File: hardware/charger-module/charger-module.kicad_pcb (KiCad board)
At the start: 4 copper layers, 80 x 24.3 mm, 74 parts, among them J1 Bus_PCI_Express_x1, J2 Conn_01x06_Pin, J3 RP_USB, J4 USB_C_Receptacle_USB2.0_14P, SW1 BOOT, SW2 RESET, U1 AMS1117-3.3, U2 W25Q32JVSSIQ, U3 RP2040, U4 MPQ4242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

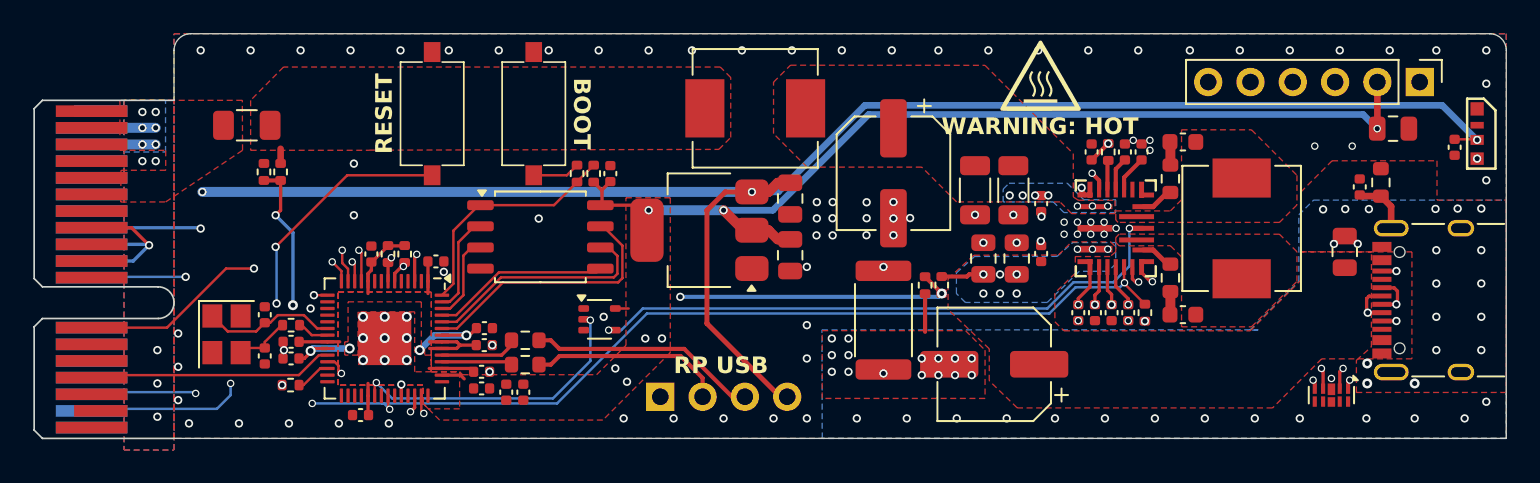
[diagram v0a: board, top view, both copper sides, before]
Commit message: feat: split i2c network
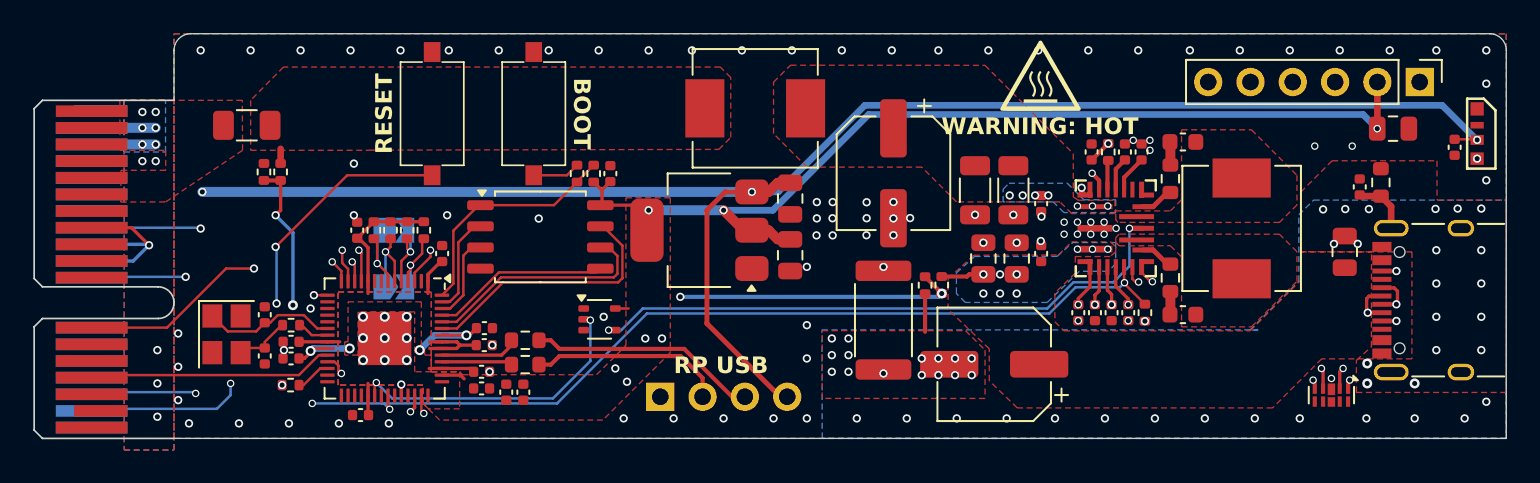
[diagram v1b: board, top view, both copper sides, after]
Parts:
- added JP1: SDA_Jumper, Jumper:SolderJumper-2_P1.3mm_Open_TrianglePad1.0x1.5mm, B.Cu at (47.2, 41.2)
- added JP2: SCL_Jumper, Jumper:SolderJumper-2_P1.3mm_Open_TrianglePad1.0x1.5mm, B.Cu at (47.2, 37.8)
- added R19: 10K, Resistor_SMD:R_0402_1005Metric, F.Cu at (49.0, 37.8)
- added R20: 10K, Resistor_SMD:R_0402_1005Metric, F.Cu at (48.0, 37.8)
- moved C24 1.66 mm to (45.0, 37.8)
- moved R12 1.66 mm to (47.0, 37.8)
- moved R13 1.66 mm to (46.0, 37.8)
- moved C18 0.61 mm to (50.1, 39.2), turned to 90 degrees
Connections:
- net LED_DIN renamed /LED_DIN
- J1 pad A8: SDA -> /SDA_IN
- J1 pad B12: SCL -> /SCL_IN
- R12 pad 2: SDA -> /SDA_IN
- R13 pad 2: SCL -> /SCL_IN
- U3 pad 4: /GPIO2 -> /SDA_OUT
- U3 pad 5: /GPIO3 -> /SCL_OUT
- U3 pad 6: SDA -> /SDA_IN
- U3 pad 7: SCL -> /SCL_IN
- U4 pad 10: SCL -> /SCL_OUT
- U4 pad 9: SDA -> /SDA_OUT
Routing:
- net SCL: track 82.2 -> 0.00 mm, vias 3 -> 0
- net SDA: track 81.4 -> 0.00 mm, vias 3 -> 0
- net /SCL_OUT: track 0.00 -> 63.9 mm, vias 0 -> 2
- net /SDA_OUT: track 0.00 -> 63.9 mm, vias 0 -> 2
- net /SDA_IN: track 0.00 -> 25.1 mm, vias 0 -> 2
- net /SCL_IN: track 0.00 -> 23.9 mm, vias 0 -> 2
- net +3.3V: track 77.0 -> 81.1 mm
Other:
- board text added: "I2C Combine"

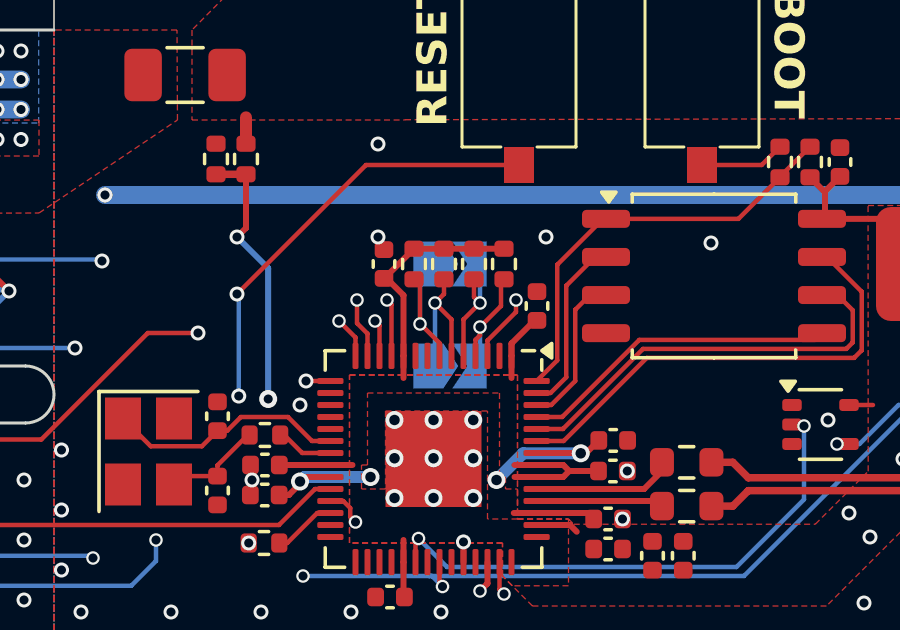
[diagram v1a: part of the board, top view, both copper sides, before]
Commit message: chore: switch jumper footprints
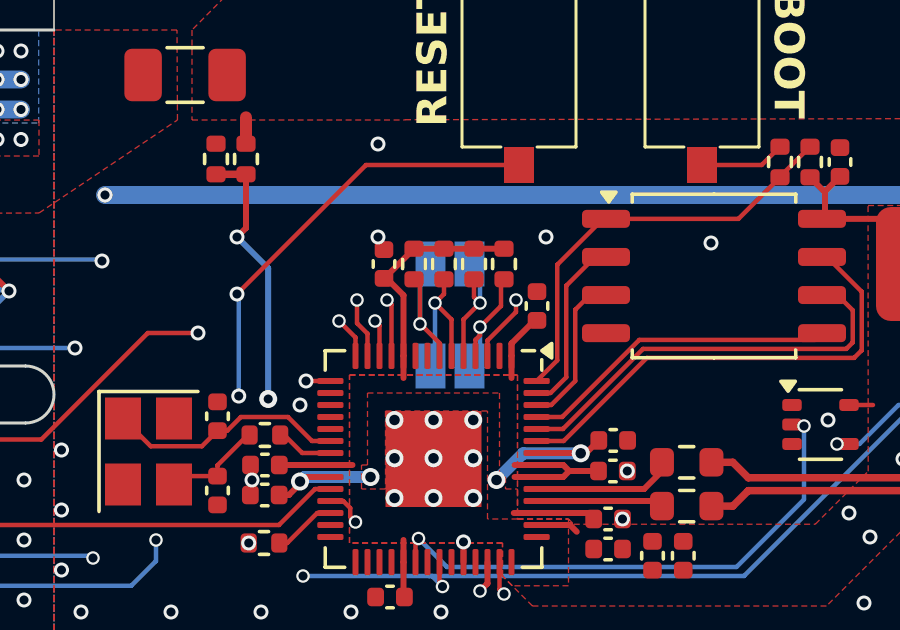
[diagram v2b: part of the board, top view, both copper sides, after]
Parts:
- JP1, JP2: footprint Jumper:SolderJumper-2_P1.3mm_Open_TrianglePad1.0x1.5mm -> Jumper:SolderJumper-2_P1.3mm_Open_Pad1.0x1.5mm
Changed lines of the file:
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@@
 		)
 	)
-	(footprint "Jumper:SolderJumper-2_P1.3mm_Open_TrianglePad1.0x1.5mm"
+	(footprint "Jumper:SolderJumper-2_P1.3mm_Open_Pad1.0x1.5mm"
 		(layer "B.Cu")
 		(at 47.2 37.8)
-		(descr "SMD Solder Jumper, 1x1.5mm Triangular Pads, 0.3mm gap, open")
+		(descr "SMD Solder Jumper, 1x1.5mm Pads, 0.3mm gap, open")
 		(tags "solder jumper open")
 		(property "Reference" "JP2"
-			(at 0 1.8 360)
-			(layer "B.SilkS")
-			(hide yes)
+			(at 0 1.8 180)
+			(layer "B.SilkS")
 			(effects
 				(font
@@
 		)
 		(property "Value" "SCL_Jumper"
-			(at 0 -1.9 360)
-			(layer "B.Fab")
-			(effects
-				(font
-					(size 1 1)
-					(thickness 0.15)
-				)
-				(justify mirror)
-			)
-		)
-		(property "Footprint" "Jumper:SolderJumper-2_P1.3mm_Open_TrianglePad1.0x1.5mm"
+			(at 0 -1.9 180)
+			(layer "B.Fab")
+			(effects
+				(font
+					(size 1 1)
+					(thickness 0.15)
+				)
+				(justify mirror)
+			)
+		)
+		(property "Footprint" "Jumper:SolderJumper-2_P1.3mm_Open_Pad1.0x1.5mm"
 			(at 0 0 180)
 			(unlocked yes)
@@
 			(layer "B.CrtYd")
 		)
-		(pad "1" smd custom
-			(at -0.725 0)
-			(size 0.3 0.3)
+		(pad "1" smd rect
+			(at -0.65 0)
+			(size 1 1.5)
 			(layers "B.Cu" "B.Mask")
 			(net 90 "/SCL_IN")
 			(pinfunction "A")
 			(pintype "passive")
-			(zone_connect 2)
-			(thermal_bridge_angle 45)
-			(options
-				(clearance outline)
-				(anchor rect)
-			)
-			(primitives
-				(gr_poly
-					(pts
-						(xy 1 0) (xy 0.5 -0.75) (xy -0.5 -0.75) (xy -0.5 0.75) (xy 0.5 0.75)
-					)
-					(width 0)
-					(fill yes)
-				)
-			)
-		)
-		(pad "2" smd custom
-			(at 0.725 0)
-			(size 0.3 0.3)
+		)
+		(pad "2" smd rect
+			(at 0.65 0)
+			(size 1 1.5)
 			(layers "B.Cu" "B.Mask")
 			(net 89 "/SCL_OUT")
 			(pinfunction "B")
 			(pintype "passive")
-			(zone_connect 2)
-			(thermal_bridge_angle 45)
-			(options
-				(clearance outline)
-				(anchor rect)
-			)
-			(primitives
-				(gr_poly
-					(pts
-						(xy 0.5 -0.75) (xy -0.65 -0.75) (xy -0.15 0) (xy -0.65 0.75) (xy 0.5 0.75)
-					)
-					(width 0)
-					(fill yes)
-				)
-			)
 		)
 	)
@@
 		)
 	)
-	(footprint "Jumper:SolderJumper-2_P1.3mm_Open_TrianglePad1.0x1.5mm"
+	(footprint "Jumper:SolderJumper-2_P1.3mm_Open_Pad1.0x1.5mm"
 		(layer "B.Cu")
 		(at 47.2 41.2)
-		(descr "SMD Solder Jumper, 1x1.5mm Triangular Pads, 0.3mm gap, open")
+		(descr "SMD Solder Jumper, 1x1.5mm Pads, 0.3mm gap, open")
 		(tags "solder jumper open")
 		(property "Reference" "JP1"
-			(at 0 1.8 360)
-			(layer "B.SilkS")
-			(hide yes)
+			(at 0 1.8 180)
+			(layer "B.SilkS")
 			(effects
 				(font
@@
 		)
 		(property "Value" "SDA_Jumper"
-			(at 0 -1.9 360)
-			(layer "B.Fab")
-			(effects
-				(font
-					(size 1 1)
-					(thickness 0.15)
-				)
-				(justify mirror)
-			)
-		)
-		(property "Footprint" "Jumper:SolderJumper-2_P1.3mm_Open_TrianglePad1.0x1.5mm"
+			(at 0 -1.9 180)
+			(layer "B.Fab")
+			(effects
+				(font
+					(size 1 1)
+					(thickness 0.15)
+				)
+				(justify mirror)
+			)
+		)
+		(property "Footprint" "Jumper:SolderJumper-2_P1.3mm_Open_Pad1.0x1.5mm"
 			(at 0 0 180)
 			(unlocked yes)
@@
 			(layer "B.CrtYd")
 		)
-		(pad "1" smd custom
-			(at -0.725 0)
-			(size 0.3 0.3)
+		(pad "1" smd rect
+			(at -0.65 0)
+			(size 1 1.5)
 			(layers "B.Cu" "B.Mask")
 			(net 87 "/SDA_IN")
 			(pinfunction "A")
 			(pintype "passive")
-			(zone_connect 2)
-			(thermal_bridge_angle 45)
-			(options
-				(clearance outline)
-				(anchor rect)
-			)
-			(primitives
-				(gr_poly
-					(pts
-						(xy 1 0) (xy 0.5 -0.75) (xy -0.5 -0.75) (xy -0.5 0.75) (xy 0.5 0.75)
-					)
-					(width 0)
-					(fill yes)
-				)
-			)
-		)
-		(pad "2" smd custom
-			(at 0.725 0)
-			(size 0.3 0.3)
+		)
+		(pad "2" smd rect
+			(at 0.65 0)
+			(size 1 1.5)
 			(layers "B.Cu" "B.Mask")
 			(net 88 "/SDA_OUT")
 			(pinfunction "B")
 			(pintype "passive")
-			(zone_connect 2)
-			(thermal_bridge_angle 45)
-			(options
-				(clearance outline)
-				(anchor rect)
-			)
-			(primitives
-				(gr_poly
-					(pts
-						(xy 0.5 -0.75) (xy -0.65 -0.75) (xy -0.15 0) (xy -0.65 0.75) (xy 0.5 0.75)
-					)
-					(width 0)
-					(fill yes)
-				)
-			)
 		)
 	)

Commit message: fix: increase i2c pullup cap
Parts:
- C24: value 100nF -> 2.2uF
